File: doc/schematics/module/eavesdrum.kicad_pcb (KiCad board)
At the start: 2 copper layers, 100 x 100 mm, 100 parts, among them J1 DC37_Pins_MountingHoles, J2 Conn_02x25_Odd_Even, J3 Conn_01x03, M4_1 MountingHole_4.3mm_M4, M4_2 MountingHole_4.3mm_M4, M4_3 MountingHole_4.3mm_M4, M4_4 MountingHole_4.3mm_M4, SW1 SW_Push, SW2 SW_Push, SW3 SW_Push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

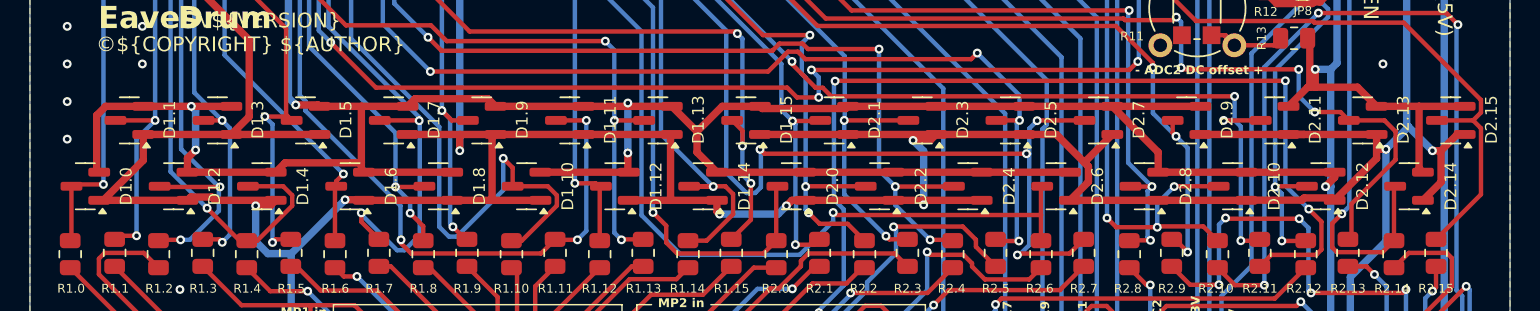
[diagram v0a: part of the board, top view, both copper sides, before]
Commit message: module schematic v1.1.1: use header instead of pico
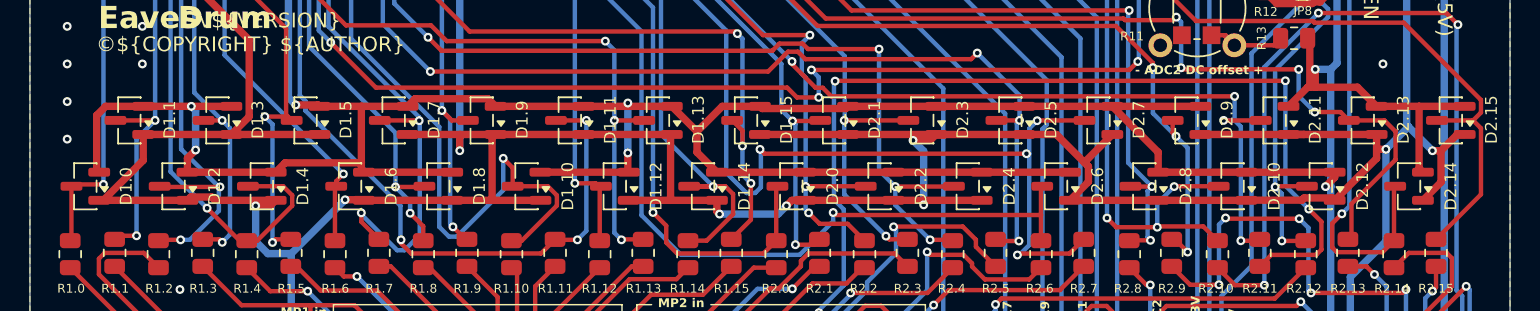
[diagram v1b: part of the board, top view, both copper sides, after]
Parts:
- added J4: Conn_01x20_Pin, Connector_PinSocket_2.54mm:PinSocket_1x20_P2.54mm_Vertical, F.Cu at (163.1, 57.5)
- added J5: Conn_01x20_Pin, Connector_PinSocket_2.54mm:PinSocket_1x20_P2.54mm_Vertical, F.Cu at (114.8, 75.3)
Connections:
- net /addr1_0 renamed gpio6
- net /addr1_1 renamed gpio7
- net /addr1_2 renamed gpio8
- net /addr1_3 renamed gpio9
- net /addr2_0 renamed gpio11
- net /addr2_1 renamed gpio12
- net /addr2_2 renamed gpio13
- net /addr2_3 renamed gpio14
- net /gpio16 renamed gpio16
- net /gpio17 renamed gpio17
- net /gpio18 renamed gpio18
- net /gpio19 renamed gpio19
- net /gpio2 renamed gpio2
- net /gpio20 renamed gpio20
- net /gpio21 renamed gpio21
- net /gpio22 renamed gpio22
- net /gpio3 renamed gpio3
- net /gpio4 renamed gpio4
- net /gpio5 renamed gpio5
- net /nEna1 renamed gpio10
- net /nEna2 renamed gpio15
- net /sel0 renamed sel0
- net /sel1 renamed sel1
- net /sel2 renamed sel2
- net /sel3 renamed sel3
- net /sel4 renamed sel4
- net Net-(A1-ADC_VREF) renamed ADC_Vref
- net Net-(A1-GPIO0) renamed gpio0
- net Net-(A1-GPIO1) renamed gpio1
- net Net-(A1-RUN) renamed run
- net pin35 renamed Net-(J2-Pin_47)
- A1 pad 37: unconnected-(A1-3V3_EN-Pad37)_2 -> 3V3_en
- A1 pad 40: unconnected-(A1-VBUS-Pad40)_1 -> Vbus
